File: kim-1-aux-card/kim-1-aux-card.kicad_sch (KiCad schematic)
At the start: 18 parts, among them J1 Motherboard, J10 RS_232, J2 SD_Shield, J4 Reset, J5 GND, J6 +5V, J6 DIN-6, Q1 PN2222A, SW1 TTY_KBD, U1 74LS06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

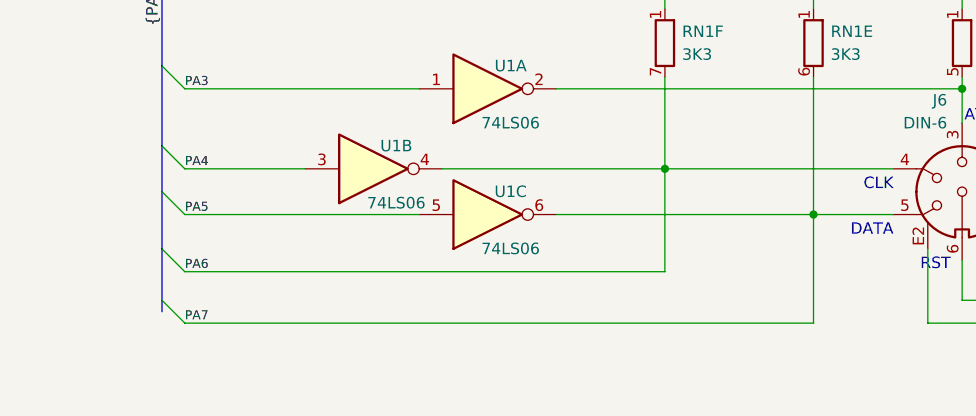
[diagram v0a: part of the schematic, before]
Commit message: Revision 3. Fixes Issue #3
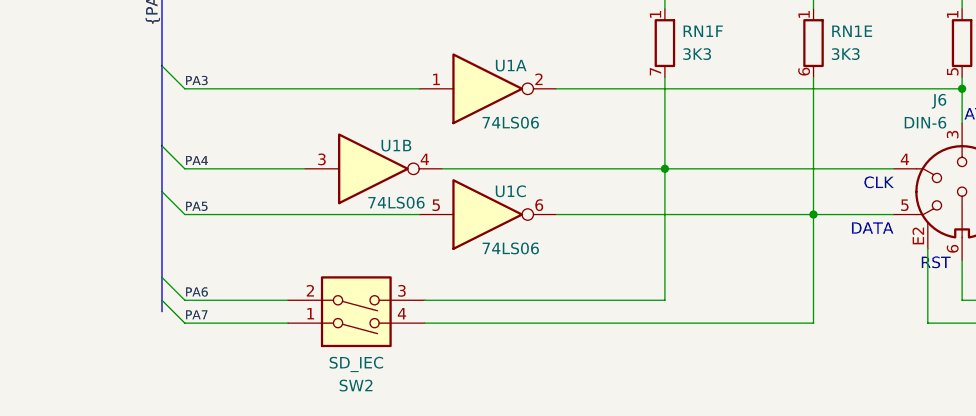
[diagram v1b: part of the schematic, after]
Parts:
- added SW2: SD_IEC, Button_Switch_THT:SW_DIP_SPSTx02_Slide_9.78x7.26mm_W7.62mm_P2.54mm, symbol Switch:SW_DIP_x02
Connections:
- net PA6: now also SW2.2; no longer J6.4, RN1.7 (R6.2), U1.4
- net PA7: now also SW2.1; no longer J6.5, RN1.6 (R5.2), U1.6
- new net: J6.4, RN1.7 (R6.2), SW2.3, U1.4
- new net: J6.5, RN1.6 (R5.2), SW2.4, U1.6
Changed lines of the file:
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@@
     (stroke (width 0) (type default))
   )
-  (bus_entry (at 49.53 222.885) (size 2.54 2.54)
+  (bus_entry (at 49.53 226.06) (size 2.54 2.54)
     (stroke (width 0) (type default))
   )
@@
     (stroke (width 0) (type default))
   )
+  (wire (pts (xy 78.74 231.14) (xy 121.92 231.14))
+    (stroke (width 0) (type default))
+  )
   (wire (pts (xy 52.07 72.39) (xy 57.15 72.39))
     (stroke (width 0) (type default))
@@
     (stroke (width 0) (type default))
   )
-  (wire (pts (xy 52.07 225.425) (xy 105.41 225.425))
+  (wire (pts (xy 52.07 228.6) (xy 63.5 228.6))
     (stroke (width 0) (type default))
   )
@@
     (stroke (width 0) (type default))
   )
-  (bus (pts (xy 49.53 222.885) (xy 49.53 228.6))
+  (bus (pts (xy 49.53 226.06) (xy 49.53 228.6))
     (stroke (width 0) (type default))
   )
@@
     (stroke (width 0) (type default))
   )
-  (bus (pts (xy 49.53 216.535) (xy 49.53 222.885))
+  (bus (pts (xy 49.53 216.535) (xy 49.53 226.06))
     (stroke (width 0) (type default))
   )
@@
     (stroke (width 0) (type default))
   )
+  (wire (pts (xy 78.74 228.6) (xy 105.41 228.6))
+    (stroke (width 0) (type default))
+  )
   (wire (pts (xy 134.62 231.14) (xy 142.24 231.14))
     (stroke (width 0) (type default))
@@
     (stroke (width 0) (type default))
   )
-  (wire (pts (xy 52.07 231.14) (xy 121.92 231.14))
+  (wire (pts (xy 52.07 231.14) (xy 63.5 231.14))
     (stroke (width 0) (type default))
   )
@@
     (stroke (width 0) (type default))
   )
-  (wire (pts (xy 105.41 225.425) (xy 105.41 213.995))
+  (wire (pts (xy 105.41 228.6) (xy 105.41 213.995))
     (stroke (width 0) (type default))
   )
@@
     (effects (font (size 1 1)) (justify left bottom))
   )
-  (label "PA6" (at 52.07 225.425 0) (fields_autoplaced)
+  (label "PA6" (at 52.07 228.6 0) (fields_autoplaced)
     (effects (font (size 1 1)) (justify left bottom))
   )
@@
         )
       )
+    )
+  )
+  (symbol (lib_id "Switch:SW_DIP_x02") (at 71.12 228.6 0) (mirror x) (unit 1)
+    (in_bom yes) (on_board yes) (dnp no)
+    (property "Reference" "SW2" (at 71.12 238.125 0)
+      (effects (font (size 1.27 1.27)))
+    )
+    (property "Value" "SD_IEC" (at 71.12 235.585 0)
+      (effects (font (size 1.27 1.27)))
+    )
+    (property "Footprint" "Button_Switch_THT:SW_DIP_SPSTx02_Slide_9.78x7.26mm_W7.62mm_P2.54mm" (at 71.12 228.6 0)
+      (effects (font (size 1.27 1.27)) hide)
+    )
+    (property "Datasheet" "~" (at 71.12 228.6 0)
+      (effects (font (size 1.27 1.27)) hide)
+    )
+    (pin "1")
+    (pin "2")
+    (pin "3")
+    (pin "4")
+    (instances
+      (project "kim-1-aux-card"
+        (path "/bccd745c-1975-422e-9da9-e7805ccc3aa8"
+          (reference "SW2") (unit 1)
+        )
+      )
